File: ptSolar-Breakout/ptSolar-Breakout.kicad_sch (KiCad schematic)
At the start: 17 parts, among them J1 6 Pin Male Header, J2 Qwiic, J3 6 Pin Male Header, J4 Conn_02x04_Odd_Even, J5 Conn_01x03, J6 Barrel_Jack_Switch, Q1 MMBT3904, SW2 SW_SPST, U1 LM1085-5.0

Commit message: Updating Bill of Materials
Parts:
- C1: value C -> Piezo Buzzer; Digikey (none) -> 102-1155-ND
- D1: value 1N4148W -> 1N4007FL; Digikey (none) -> 1655-1N4007FLCT-ND
- J1: value 6 Pin Male Header -> 6 Pin Female Socket; Digikey 732-5394-ND -> 952-1781-ND
- J4: value Conn_02x04_Odd_Even -> 8 Pin Female Socket; Digikey (none) -> 952-1790-ND
- J5: value Conn_01x03 -> 3 Pin Male Header; Digikey (none) -> 732-5316-ND
- J6: Digikey (none) -> CP-002AHPJCT-ND
- SW2: value SW_SPST -> Reset Switch; Digikey (none) -> CKN9104CT-ND
- U1: value LM1085-5.0 -> LM1086-5.0; Digikey (none) -> LM1086ISX-5.0/NOPBCT-ND
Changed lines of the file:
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@@
+			)
+		)
+		(property "Digikey" "CP-002AHPJCT-ND "
+			(at 58.42 87.63 0)
+			(effects
+				(font
+					(size 1.27 1.27)
+				)
+				(hide yes)
 			)
 		)
@@
 			)
 		)
-		(property "Value" "6 Pin Male Header"
+		(property "Value" "6 Pin Female Socket"
 			(at 171.4499 78.74 90)
 			(effects
@@
 			)
 		)
-		(property "Digikey" "732-5394-ND"
+		(property "Digikey" "952-1781-ND"
 			(at 171.45 83.82 0)
 			(effects
@@
 			)
 		)
-		(property "Value" "Conn_01x03"
+		(property "Value" "3 Pin Male Header"
 			(at 85.09 121.92 0)
 			(effects
@@
 		)
 		(property "Description" "Generic connector, single row, 01x03, script generated (kicad-library-utils/schlib/autogen/connector/)"
+			(at 85.09 115.57 0)
+			(effects
+				(font
+					(size 1.27 1.27)
+				)
+				(hide yes)
+			)
+		)
+		(property "Digikey" "732-5316-ND"
 			(at 85.09 115.57 0)
 			(effects
@@
 			)
 		)
-		(property "Value" "Conn_02x04_Odd_Even"
+		(property "Value" "8 Pin Female Socket"
 			(at 118.11 109.22 0)
 			(effects
@@
 		)
 		(property "Description" "Generic connector, double row, 02x04, odd/even pin numbering scheme (row 1 odd numbers, row 2 even numbers), script generated (kicad-library-utils/schlib/autogen/connector/)"
+			(at 116.84 115.57 0)
+			(effects
+				(font
+					(size 1.27 1.27)
+				)
+				(hide yes)
+			)
+		)
+		(property "Digikey" "952-1790-ND"
 			(at 116.84 115.57 0)
 			(effects
@@
 			)
 		)
-		(property "Value" "SW_SPST"
+		(property "Value" "Reset Switch"
 			(at 214.63 85.09 0)
 			(effects
@@
 		)
 		(property "Description" "Single Pole Single Throw (SPST) switch"
+			(at 214.63 88.9 0)
+			(effects
+				(font
+					(size 1.27 1.27)
+				)
+				(hide yes)
+			)
+		)
+		(property "Digikey" "CKN9104CT-ND"
 			(at 214.63 88.9 0)
 			(effects
@@
 			)
 		)
-		(property "Value" "C"
+		(property "Value" "Piezo Buzzer"
 			(at 180.34 130.8099 0)
 			(effects
@@
 		)
 		(property "Description" "Unpolarized capacitor"
+			(at 176.53 129.54 0)
+			(effects
+				(font
+					(size 1.27 1.27)
+				)
+				(hide yes)
+			)
+		)
+		(property "Digikey" "102-1155-ND"
 			(at 176.53 129.54 0)
 			(effects
@@
 			)
 		)
-		(property "Value" "1N4148W"
+		(property "Value" "1N4007FL"
 			(at 168.91 129.5399 90)
 			(effects
@@
 			)
 		)
-		(property "Datasheet" "https://www.vishay.com/docs/85748/1n4148w.pdf"
+		(property "Datasheet" ""
 			(at 166.37 128.27 0)
 			(effects
@@
 		(property "Sim.Pins" "1=K 2=A"
 			(at 166.37 128.27 0)
+			(effects
+				(font
+					(size 1.27 1.27)
+				)
+				(hide yes)
+			)
+		)
+		(property "Digikey" "1655-1N4007FLCT-ND"
+			(at 166.37 128.27 90)
 			(effects
 				(font
@@
 			)
 		)
-		(property "Value" "LM1085-5.0"
+		(property "Value" "LM1086-5.0"
 			(at 99.06 81.28 0)
 			(effects
@@
 			)
 		)
-		(property "Datasheet" "http://www.ti.com/lit/ds/symlink/lm1085.pdf"
+		(property "Datasheet" ""
 			(at 99.06 85.09 0)
 			(effects
@@
 			(at 99.06 85.09 0)
 			(effects
+				(font
+					(size 1.27 1.27)
+				)
+				(hide yes)
+			)
+		)
+		(property "Digikey" "LM1086ISX-5.0/NOPBCT-ND"
+			(at 99.06 85.09 0)
+			(effects

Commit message: Minor updates to the BOMs and schematics. Updates to Firmware for further testing.
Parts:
- C3: Digikey 445-1420-2-ND -> 445-1420-1-ND
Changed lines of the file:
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@@
 			)
 		)
-		(property "Digikey" "445-1420-2-ND"
+		(property "Digikey" "445-1420-1-ND"
 			(at 114.3 88.9 0)
 			(effects

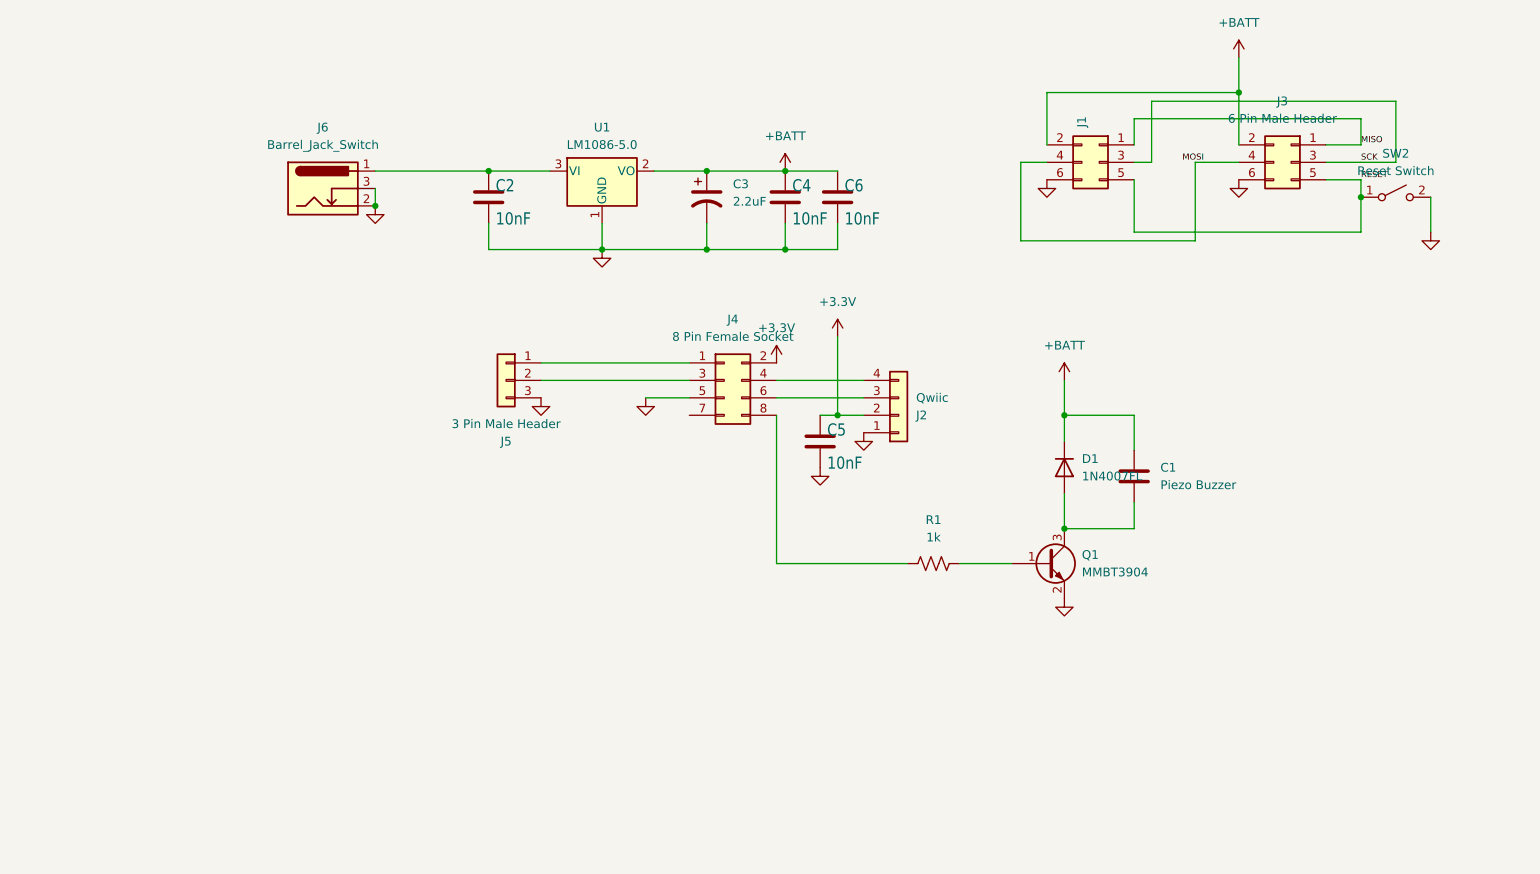
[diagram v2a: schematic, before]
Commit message: Updated Breakboard to v1.1.1. Added BME280 on board. Improved silkscreening. Updated to Kicad v9.
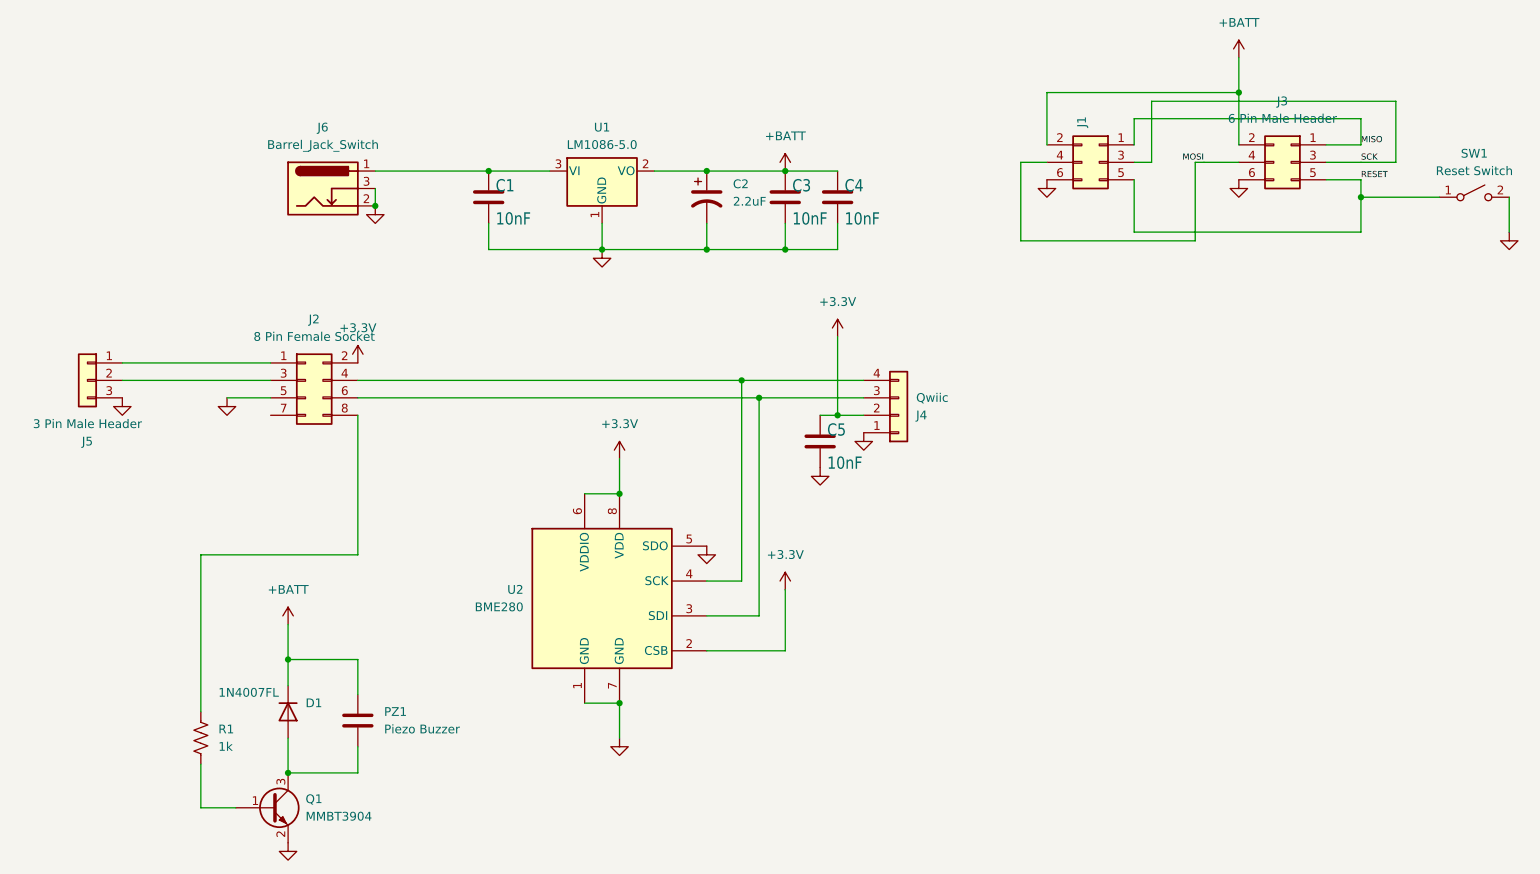
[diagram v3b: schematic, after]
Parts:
- added U2: BME280, Package_LGA:Bosch_LGA-8_2.5x2.5mm_P0.65mm_ClockwisePinNumbering, symbol Sensor:BME280
- PZ1: renamed from C1; footprint Capacitor_THT:CP_Radial_D12.5mm_P7.50mm -> Buzzer_Beeper:Buzzer_TDK_PS1240P02BT_D12.2mm_H6.5mm
- SW1: renamed from SW2; footprint Button_Switch_SMD:SW_SPST_B3S-1000 -> Button_Switch_SMD:SW_SPST_PTS647_Sx38
- renumbered C2 to C1, C3 to C2, C4 to C3, C6 to C4, J4 to J2, J2 to J4
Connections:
- net +3.3V: now also U2.2 (CSB), U2.6 (VDDIO), U2.8 (VDD)
- net GND: now also U2.1 (GND), U2.5 (SDO), U2.7 (GND)
- net at J2.6 (Pin_6), J4.3 (Pin_3): now also U2.3 (SDI)
- net at J2.4 (Pin_4), J4.4 (Pin_4): now also U2.4 (SCK)
- net at Q1.1 (B): now also R1.1; no longer R1.2
- net at J2.8 (Pin_8): now also R1.2; no longer R1.1
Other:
- moved on the sheet: D1, J2, J5, PZ1, Q1, R1, SW1

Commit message: Updated v1.1.2 with FET switch to shut down GPS. Generated Gerbers and sent off for manufacture.
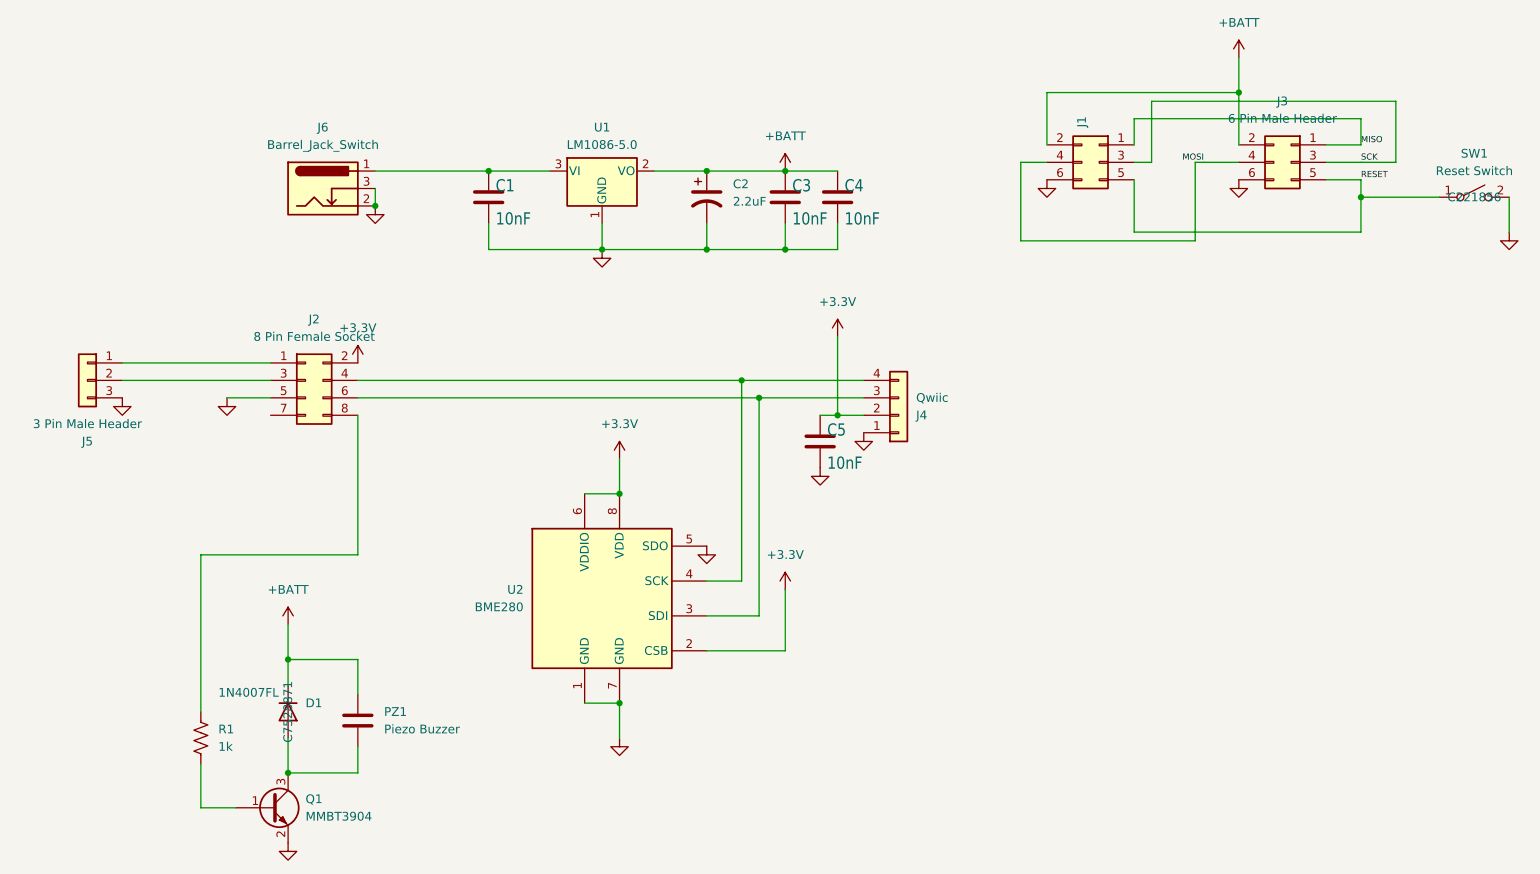
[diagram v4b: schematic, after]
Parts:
- C1, C3, C4, C5: LCSC (none) -> C83170
- C2: LCSC (none) -> C107128
- D1: LCSC (none) -> C7528871
- J4: LCSC (none) -> C160404
- J6: LCSC (none) -> C22434687
- Q1: LCSC (none) -> C81464
- R1: LCSC (none) -> C95781
- SW1: LCSC (none) -> C221856
- U1: LCSC (none) -> C5145331
- U2: LCSC (none) -> C92489
